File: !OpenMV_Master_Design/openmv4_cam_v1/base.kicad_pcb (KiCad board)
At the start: 4 copper layers, 129.6 x 57.7 mm, 58 parts, among them J5 XF2M-1015-1A, Q1 BSS138, Q2 Si2301BDS, U1 STM32H743VIT6, U2 OV7725, U5 TPS731XX, U8 PAM2305AABADJ, X1 MF-CON-MICROUSB-RIGHT, X2 USD-1040310811, Y1 7S-12.000MAHE-T

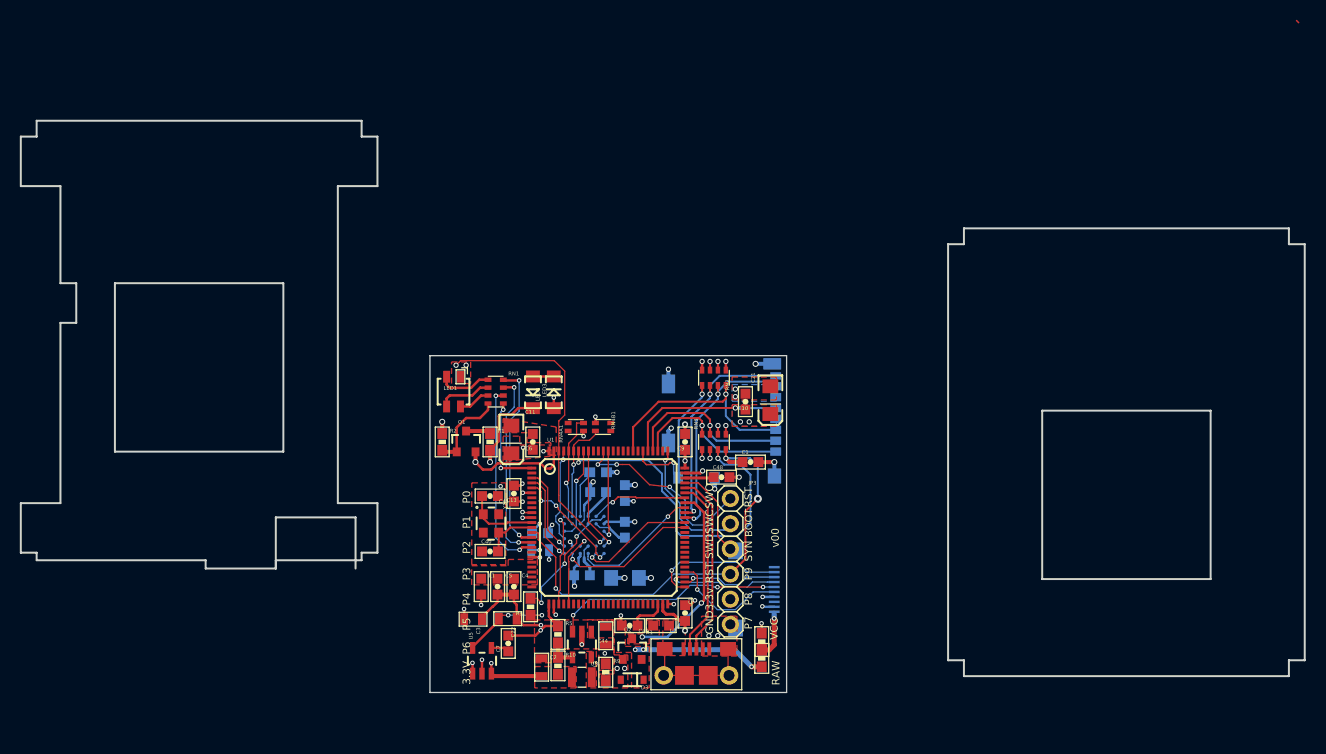
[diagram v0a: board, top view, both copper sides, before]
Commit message: Moved the flat flex connector to suit main board design
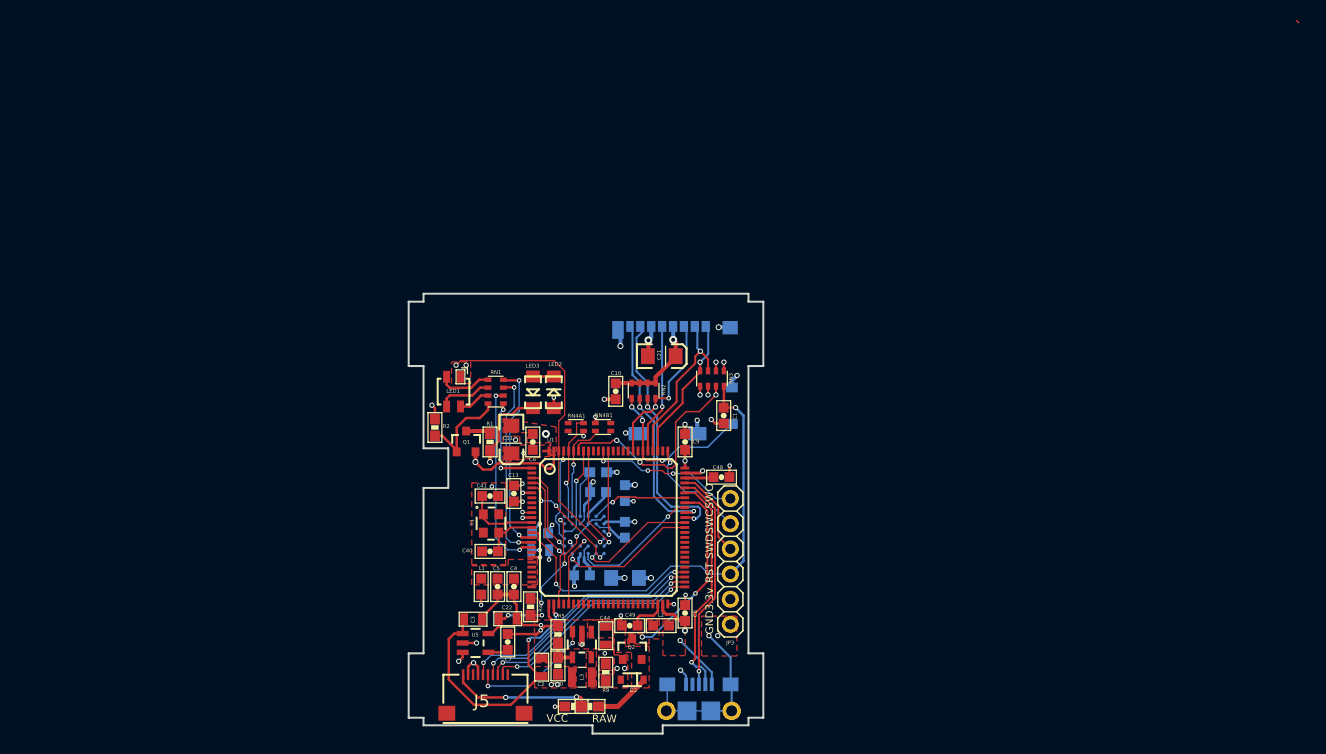
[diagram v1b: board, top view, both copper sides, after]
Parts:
- J5: footprint XF2M-1015-1A:XF2M-1015-1A -> base:XF2M-1015-1A; moved to F.Cu
- USB: renamed from X1; moved to B.Cu
- moved J5 30.4 mm to (136.1, 125.7), turned to 0 degrees
- moved R7 20.1 mm to (145.0, 128.9), turned to 0 degrees
- moved R6 18.0 mm to (146.7, 128.9), turned to 0 degrees
- moved X2 16.8 mm to (149.2, 90.3), turned to 0 degrees
- moved C10 13.1 mm to (149.2, 97.1), turned to 270 degrees
- moved C21 11.8 mm to (153.9, 93.5), turned to 0 degrees
- moved RN2 7.22 mm to (152.1, 97.0)
- moved RN3 6.40 mm to (159.0, 95.8)
- moved C1 5.41 mm to (160.2, 99.5), turned to 270 degrees
- moved USB 3.59 mm to (157.7, 128.0), turned to 180 degrees
- moved U5 1.91 mm to (135.1, 122.5), turned to 270 degrees
- moved R2 1.64 mm to (131.0, 100.8)
- moved C7 0.16 mm to (138.3, 122.4)
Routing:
- net VCC: track 32.0 -> 58.9 mm, vias 32 -> 28
- net /SPI2_SCLK: track 9.83 -> 23.2 mm, vias 1 -> 2
- net /SPI2_MOSI: track 12.1 -> 25.3 mm, vias 1 -> 2
- net /SPI2_MISO: track 11.5 -> 24.1 mm, vias 1 -> 2
- net /BOOT0: track 34.6 -> 22.3 mm, vias 2 -> 3
- net /PWR_EN: track 23.3 -> 12.7 mm, vias 3 -> 2
- net Net-(J5-Pad1): track 4.69 -> 14.3 mm, vias 1 -> 2
- net /SPI2_NSS: track 13.8 -> 22.4 mm, vias 1 -> 2
- net RAW: track 13.5 -> 5.73 mm, vias 3 -> 0
- net GND: track 75.9 -> 83.4 mm, vias 36 -> 37
- net /SDIO_CMD: track 22.1 -> 16.2 mm, vias 1 -> 2
- net Net-(X1-PadS1): track 12.0 -> 17.9 mm, vias 0 -> 1
- net Net-(L2-Pad1): track 0.00 -> 5.76 mm, vias 0 -> 1
- net /FS_DM: track 18.0 -> 22.8 mm, vias 0 -> 1
- net /SPI3_SCLK/TRACESWO: track 19.5 -> 15.4 mm
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- removed copper zone on B.Cu, net GND
- removed copper zone on B.Cu, net VCC
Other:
- board size 129.6 x 57.7 mm -> 35.8 x 44.4 mm
- board text removed: "3.3V"
- board text removed: "BOOT"
- board text removed: "Built by MacroFab"
- board text removed: "LED1=Red"
- board text removed: "LED2=Green"
- board text removed: "LED3=Blue"
- board text removed: "LED4=IR"
- board text removed: "Made in USA"
- board text removed: "P0"
- board text removed: "P1"
- board text removed: "P2"
- board text removed: "P3"
- board text removed: "P4"
- board text removed: "P5"
- board text removed: "P6"
- board text removed: "P7"
- board text removed: "P8"
- board text removed: "P9"
- board text removed: "SYN"
- board text removed: "VIN"
- board text removed: "v00"
